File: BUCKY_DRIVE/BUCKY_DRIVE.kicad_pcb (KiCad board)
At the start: 2 copper layers, 190 x 162.2 mm, 17 parts, among them J1 Conn_01x10, J2 MAG_CONN, U1 IFX9201SG_BO, U2 IFX9201SG_BO, U3 IFX9201SG_BO, U9 PCA9548ADB

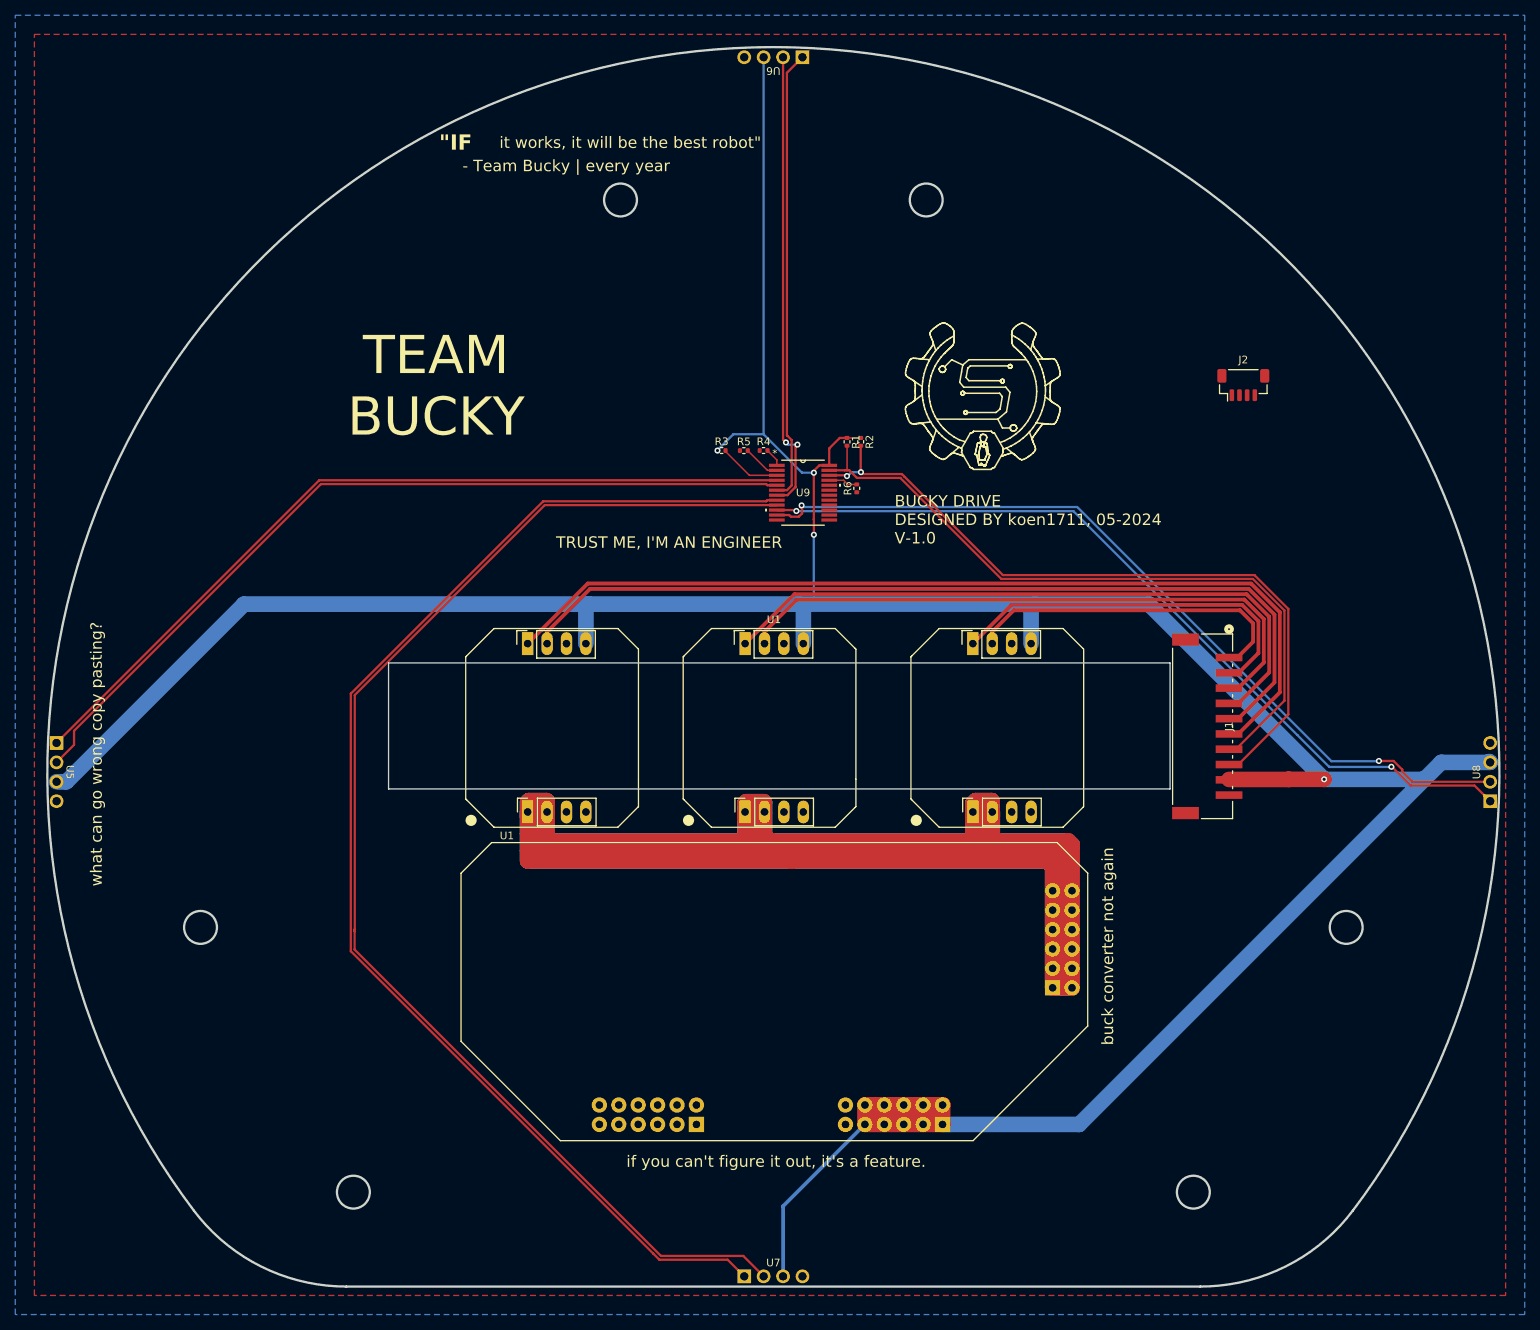
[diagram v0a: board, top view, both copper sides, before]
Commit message: chore: start on ldr instead of Q_Photo_N, interrupt instead of analog multiplexer. And a signal for front,back,left,right
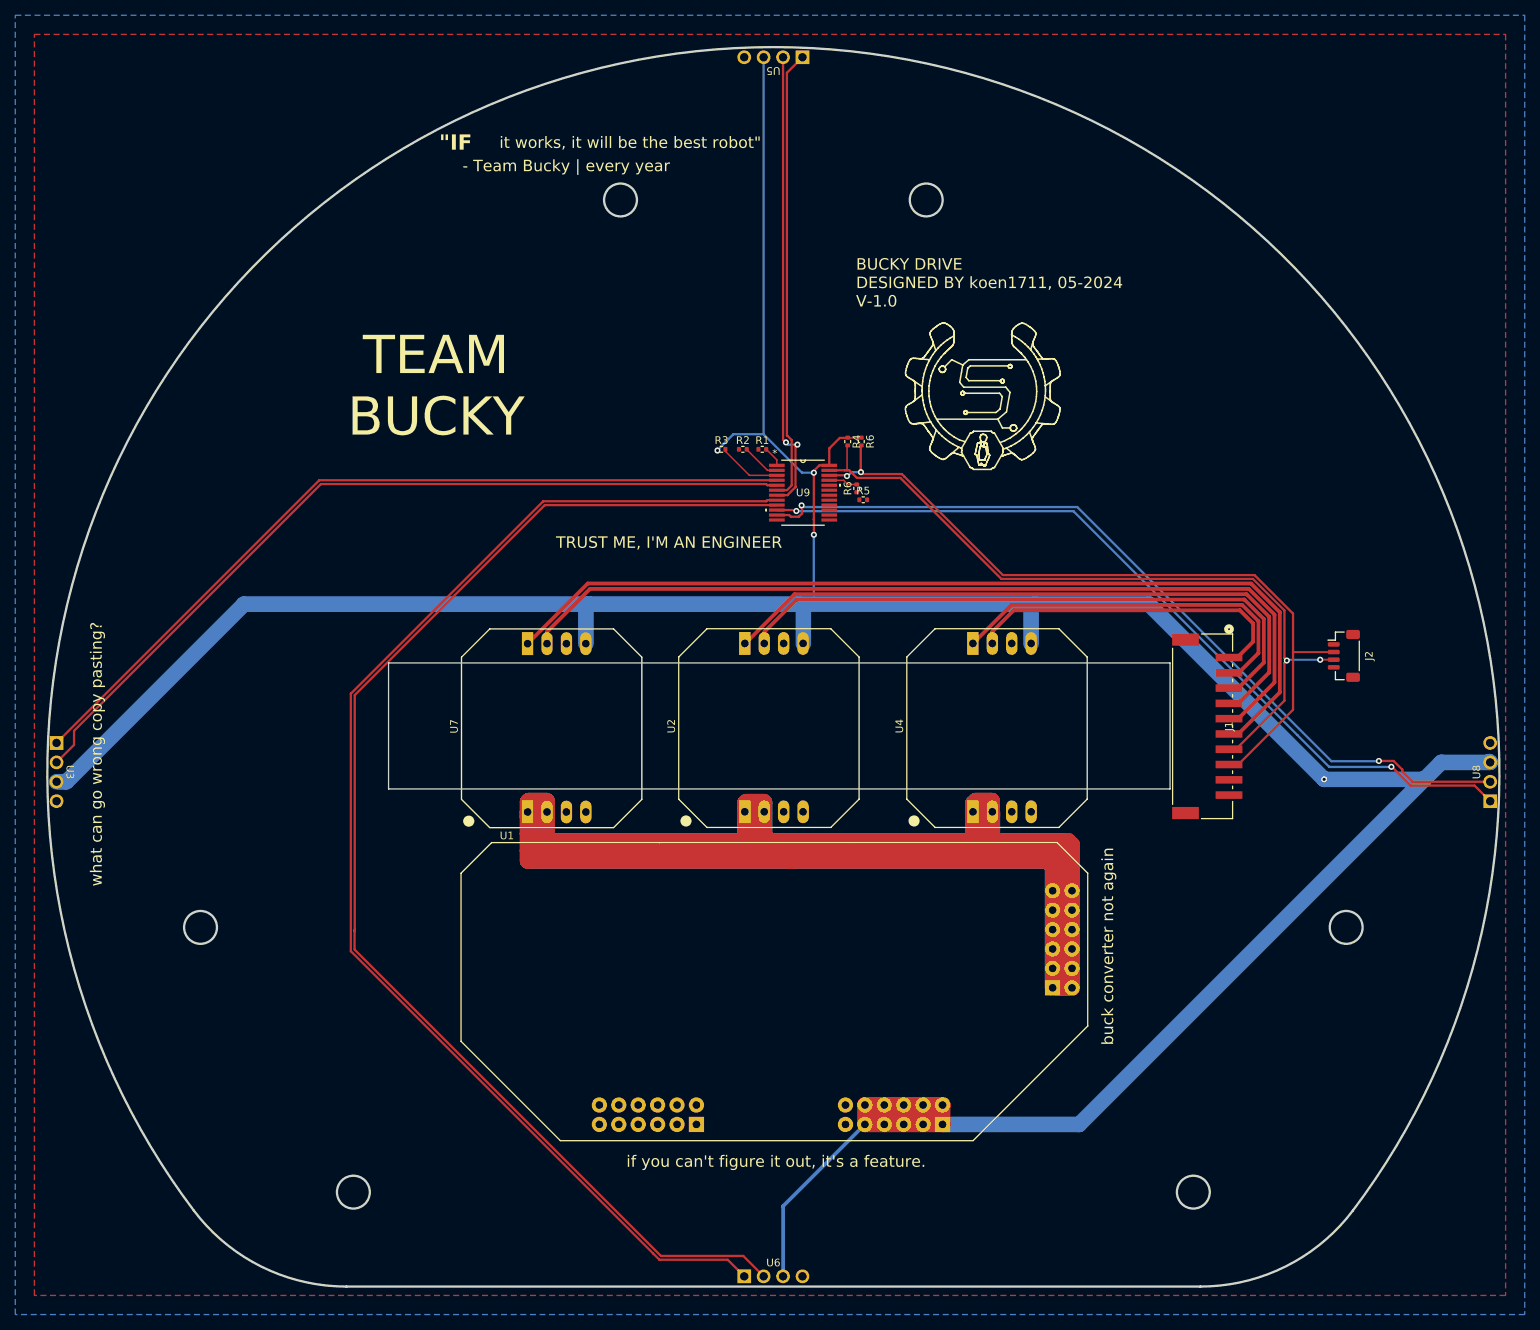
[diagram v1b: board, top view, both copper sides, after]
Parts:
- removed the U1 at (146.7, 106.0)
- added R6: 4.7kOhm, Resistor_SMD:R_0402_1005Metric, F.Cu at (158.1, 68.5)
- added U4: IFX9201SG_BO, BUCKY_DRIVE:IFX9201SG_BO, F.Cu at (176.6, 105.8)
- R1, R2: value 4700R -> 10kOhm
- R3, R5: value 10000R -> 10kOhm
- R4: value 10000R -> 4.7kOhm
- U3: value IFX9201SG_BO -> ~; footprint BUCKY_DRIVE:IFX9201SG_BO -> BUCKY_DRIVE:BUCKY_TOF
- U7: value ~ -> IFX9201SG_BO; footprint BUCKY_DRIVE:BUCKY_TOF -> BUCKY_DRIVE:IFX9201SG_BO
- moved U6 157.0 mm to (146.6, 176.5), turned to 0 degrees
- moved U5 130.7 mm to (146.6, 19.5), turned to 180 degrees
- moved U7 76.1 mm to (118.3, 105.8), turned to 90 degrees
- moved U3 64.4 mm to (54.1, 111.8), turned to -90 degrees
- moved J2 37.8 mm to (221.3, 96.6), turned to -90 degrees
- moved U2 29.7 mm to (146.8, 105.8)
- moved R5 16.9 mm to (158.4, 76.2)
- moved R2 15.5 mm to (142.6, 69.6), turned to 0 degrees
- moved R1 11.1 mm to (145.2, 69.6), turned to 0 degrees
- moved R4 11.1 mm to (156.3, 68.5), turned to -90 degrees
- moved R3 0.16 mm to (139.8, 69.6)
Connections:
- J1 pad 1: /CONNECTORS/M2_PWM -> /M2_PWM
- J1 pad 2: /CONNECTORS/M2_DIR -> /M2_DIR
- J1 pad 3: /CONNECTORS/M1_PWM -> /M1_PWM
- J1 pad 4: /CONNECTORS/M1_DIR -> /M1_DIR
- J1 pad 5: /CONNECTORS/M3_PWM -> /M3_PWM
- J1 pad 6: /CONNECTORS/M3_DIR -> /M3_DIR
- J1 pad 7: /CONNECTORS/SDA -> /SDA
- J1 pad 8: /CONNECTORS/SCL -> /SCL
- R1 pad 1: +5V -> GND
- R1 pad 2: /SDA -> Net-(U9-A0)
- R2 pad 1: +5V -> GND
- R2 pad 2: /SCL -> Net-(U9-A1)
- R4 pad 1: GND -> +5V
- R4 pad 2: Net-(U9-A0) -> /SDA
- R5 pad 2: Net-(U9-A1) -> Net-(U9-A2)
- U2 pad 5: /M2_DIR -> /M1_DIR
- U2 pad 6: /M2_PWM -> /M1_PWM
- U2 pad 7: unconnected-(U2-EN-Pad7) -> +12V
- U3 pad 1: +12V -> /SDA_0
- U3 pad 2: +12V -> /SCL_0
- U3 pad 3: GND -> +5V
- U5 pad 1: /SDA_0 -> /SDA_1
- U5 pad 2: /SCL_0 -> /SCL_1
- U6 pad 1: /SDA_1 -> /SDA_2
- U6 pad 2: /SCL_1 -> /SCL_2
- U7 pad 1: /SDA_2 -> +12V
- U7 pad 2: /SCL_2 -> +12V
- U7 pad 3: +5V -> GND
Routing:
- net +5V: track 504.5 -> 492.0 mm
- net /SDA: track 92.0 -> 98.5 mm, vias 0 -> 2
- net /SCL: track 95.6 -> 101.4 mm

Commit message: chore: convert 2 layer DRIVE -> 4 layer
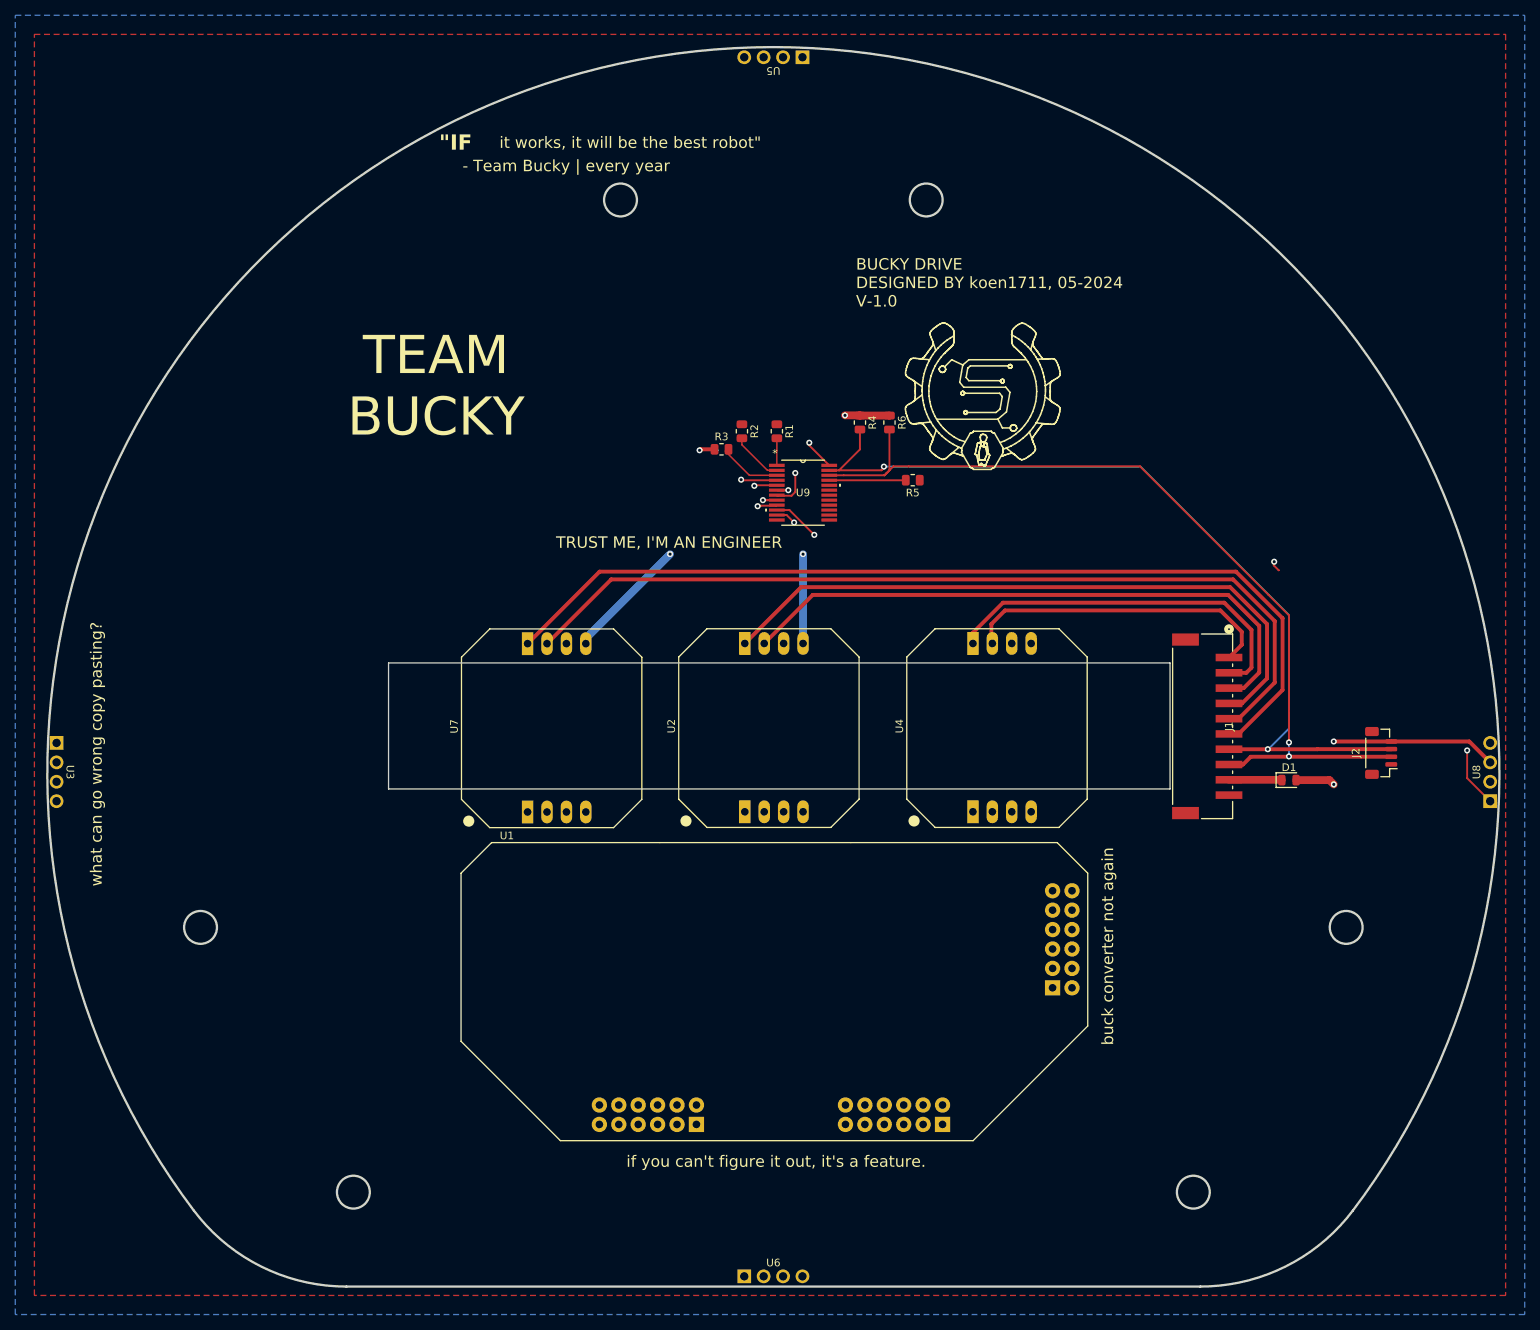
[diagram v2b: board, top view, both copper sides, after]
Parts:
- removed the R6 at (157.5, 74.7)
- removed the R6 at (158.1, 68.5)
- added D1: D, Diode_SMD:D_0805_2012Metric, F.Cu at (214.1, 112.8)
- added R6: 4.7kOhm, Resistor_SMD:R_0805_2012Metric, F.Cu at (161.8, 66.0)
- R1, R2, R3, R4, R5: footprint Resistor_SMD:R_0402_1005Metric -> Resistor_SMD:R_0805_2012Metric
- moved J2 13.6 mm to (226.1, 109.3), turned to 90 degrees
- moved R5 6.97 mm to (164.8, 73.6), turned to 180 degrees
- moved R1 3.03 mm to (147.1, 67.2), turned to -90 degrees
- moved R4 2.96 mm to (157.9, 66.0)
- moved R2 2.37 mm to (142.5, 67.2), turned to -90 degrees
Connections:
- J2 pad 4: +3.3V -> +5V
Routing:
- net +12V: track 692.1 -> 121.4 mm
- net /SDA: track 98.5 -> 115.2 mm
- net /SCL: track 101.4 -> 115.1 mm
- net /SDA_2: track 169.0 -> 177.4 mm, vias 0 -> 1
- net /SCL_2: track 170.1 -> 177.9 mm, vias 0 -> 1
- net Net-(D1-K): track 0.00 -> 6.92 mm
- net Net-(U9-A2): track 3.83 -> 10.0 mm
- net +5V: track 492.0 -> 496.4 mm, vias 4 -> 7
- net /M2_PWM: track 43.9 -> 41.3 mm
- net Net-(U9-A1): track 4.87 -> 6.81 mm
- net /SDA_3: track 109.5 -> 111.4 mm
- net /SCL_3: track 111.0 -> 109.2 mm
- net /M3_DIR: track 122.6 -> 124.0 mm
- net /M1_PWM: track 81.3 -> 80.0 mm
- net /SCL_0: track 110.5 -> 109.3 mm, vias 0 -> 1
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- added copper zone on In1.Cu, net +12V
- added copper zone on In1.Cu, net GND
- added copper zone on In2.Cu, net GND
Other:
- copper layers 2 -> 4

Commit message: chore: make all PCBs from 2 layers to 4 layers
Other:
- board text added: "BUCKY DRIVE DESIGNED BY koen1711, 09-2024 V-1.0"
- board text removed: "BUCKY DRIVE DESIGNED BY koen1711, 05-2024 V-1.0"

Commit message: fix all drc issues
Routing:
- net /SCL_3: track 109.2 -> 107.8 mm, vias 2 -> 1

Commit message: fix: BUCKY_MAIN v2?
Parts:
- added J2: Conn_01x01, Connector_PinHeader_2.54mm:PinHeader_1x01_P2.54mm_Vertical, F.Cu at (128.4, 63.8)
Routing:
- net +5V: track 496.3 -> 103.9 mm, vias 7 -> 6
- net +12V: track 121.4 -> 0.00 mm
- net /SCL: track 115.1 -> 117.8 mm
- net /SCL_2: track 177.9 -> 180.0 mm
- net /SCL_3: track 107.8 -> 109.5 mm
- net /SDA_3: track 111.5 -> 109.9 mm
- net /SDA_2: track 177.4 -> 178.4 mm
- net /SDA_0: track 108.5 -> 109.5 mm
- added copper zone on B.Cu, net +12V
- added copper zone on In1.Cu, net +5V
- removed copper zone on In1.Cu, net +12V
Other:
- board text added: "THE BEAUTIFUL GAME"
- board text added: "hard work beats talent any day, but if you're talented and work hard, it's hard to be beat - my girlfriend, oh wait she doesn't exist"
- board text removed: "TRUST ME, I'M AN ENGINEER"
- board text removed: "buck converter not again"
- board text removed: "if you can't figure it out, it's a feature."
